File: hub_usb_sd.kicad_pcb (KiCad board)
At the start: 4 copper layers, 50 x 50 mm, 66 parts, among them J1 Downstream_2, J2 Downstream_3, J3 I²C, J4 Upstream, J5 SD_Card, J6 EEPROM_Pgm, J7 External_Power, U1 USB2642-I_ML, U2 TPS2052C, U3 AT24CS04BN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

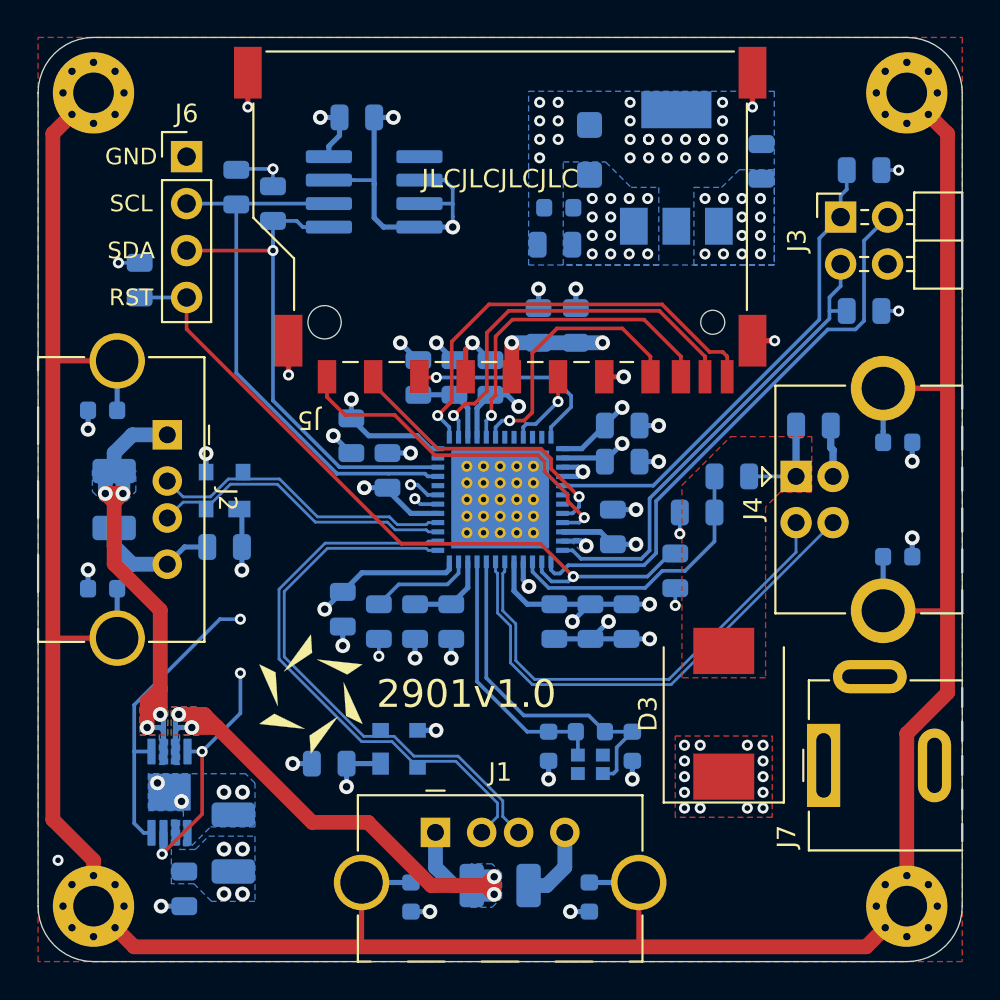
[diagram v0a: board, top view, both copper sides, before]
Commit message: Upgraded project to Kicad 8.0. Defined part# fields. Further corrections pending
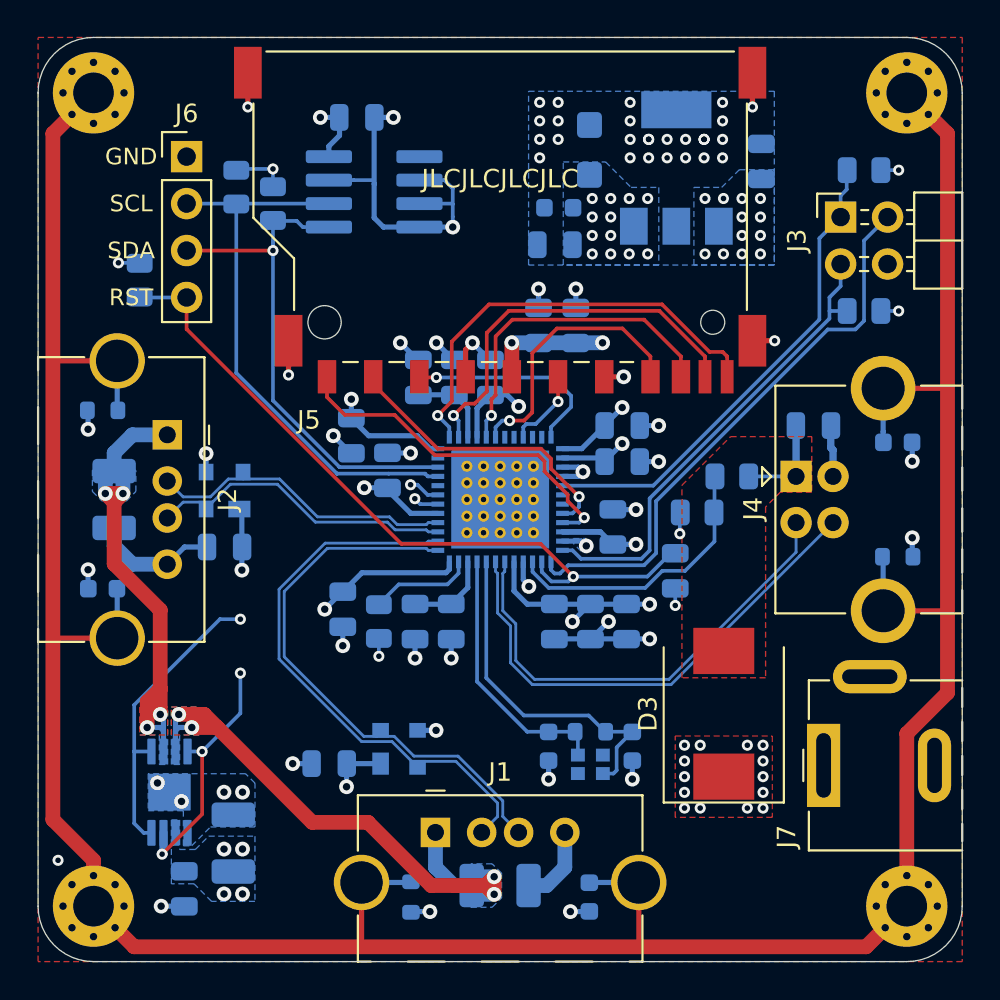
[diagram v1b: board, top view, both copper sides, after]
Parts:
- removed G***: Project_ID_2400dpi, Extra:Project_ID_2400dpi
- U3: value AT24CS04BN -> AT24C04
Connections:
- U1 pad 11: (no net) -> unconnected-(U1-SPI_DI-Pad11)
- U1 pad 19: (no net) -> unconnected-(U1-SD_D7-Pad19)
- U1 pad 20: (no net) -> unconnected-(U1-SD_D6-Pad20)
- U1 pad 22: (no net) -> unconnected-(U1-REG_EN-Pad22)
- U1 pad 23: (no net) -> unconnected-(U1-SD_D5-Pad23)
- U1 pad 30: (no net) -> unconnected-(U1-SD_D4-Pad30)
- U1 pad 31: (no net) -> unconnected-(U1-NC-Pad31)
- U1 pad 8: (no net) -> unconnected-(U1-~{SPI_CE}-Pad8)
- U3 pad 1: (no net) -> unconnected-(U3-A0-Pad1)
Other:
- net class Default removed
- net class DiffZ90 removed
